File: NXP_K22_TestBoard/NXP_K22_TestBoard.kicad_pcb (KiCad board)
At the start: 4 copper layers, 60 x 90 mm, 63 parts, among them J301 Barrel_Jack, J302 Conn_ARM_JTAG_SWD_10, J303 PortA, J304 PortB, J305 PortC, J306 PortD, J307 Analog, J308 OLED, J309 UART, J310 Power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

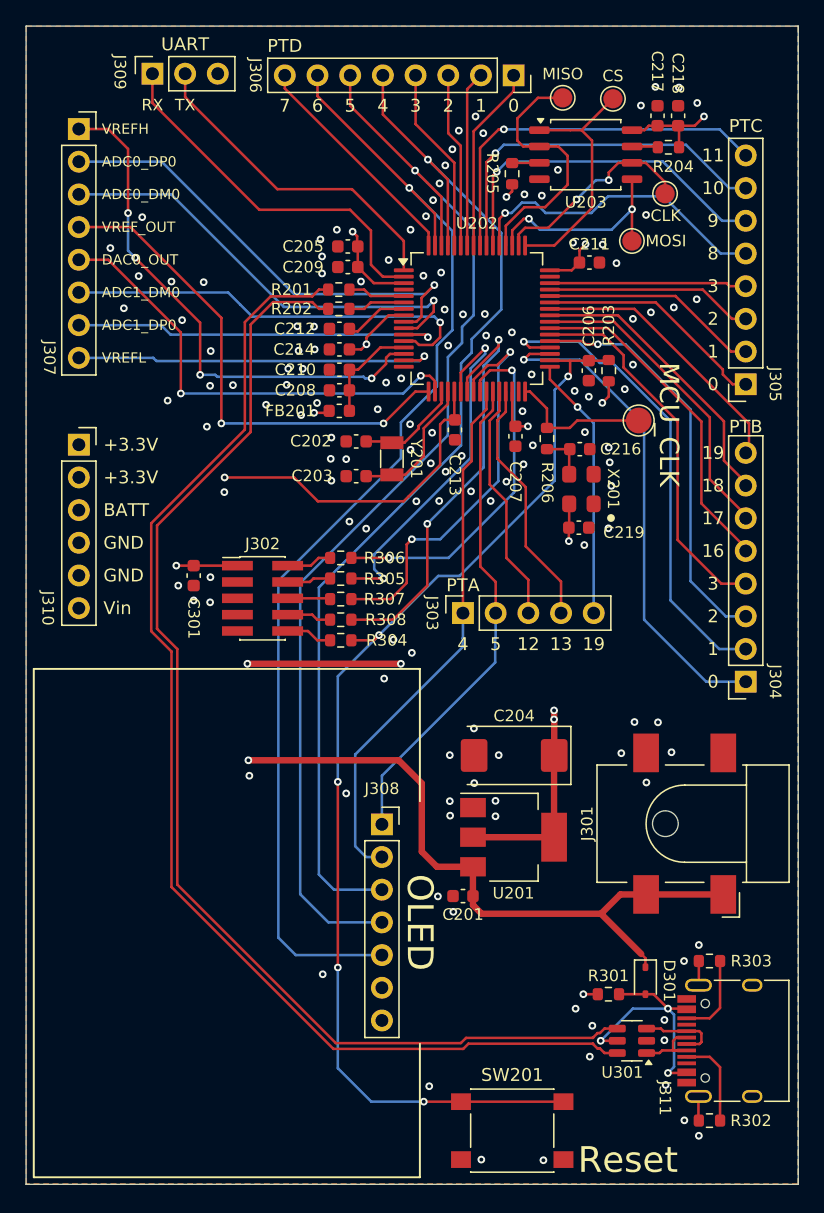
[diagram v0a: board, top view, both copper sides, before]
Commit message: Finished board layout
Design rules not checked yet
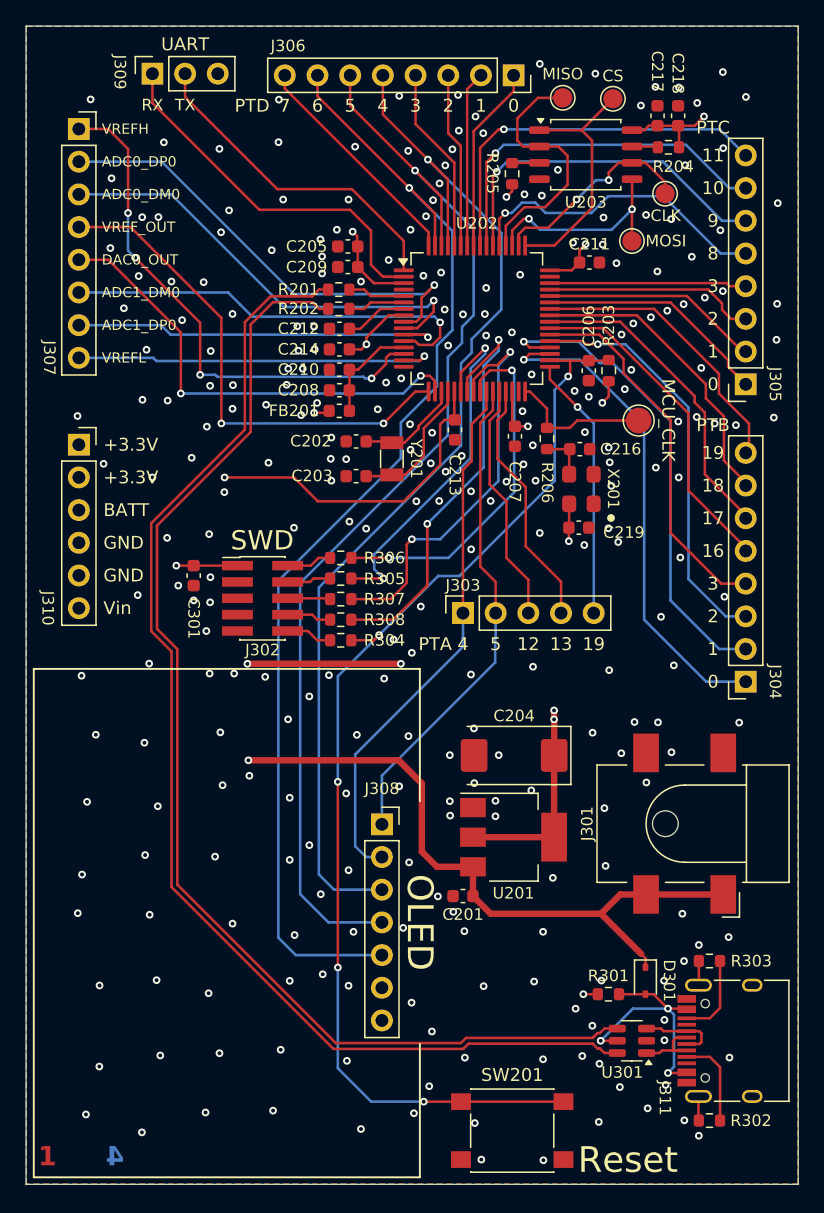
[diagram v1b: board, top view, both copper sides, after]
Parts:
- added REF**: Symbol_Barrel_Polarity, Symbol:Symbol_Barrel_Polarity, B.Cu at (144.3, 94.8)
- C202, C203: value C -> 20p
- C217: value 1nF -> 1n
- C218: value 100nF -> 100n
- C301: value C -> 100n
- Y201: value Crystal -> 32.768 kHz
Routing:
- net PTC2: track 16.3 -> 17.2 mm
- net PTB19: track 21.4 -> 22.3 mm
- net PTB18: track 22.7 -> 23.5 mm
- net GND: vias 133 -> 274
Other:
- board text added: "+"
- board text added: "-"
- board text added: "NXP MK22FN512 Test board V1.0 by Morgan ON4MOD"
- board text added: "SWD"

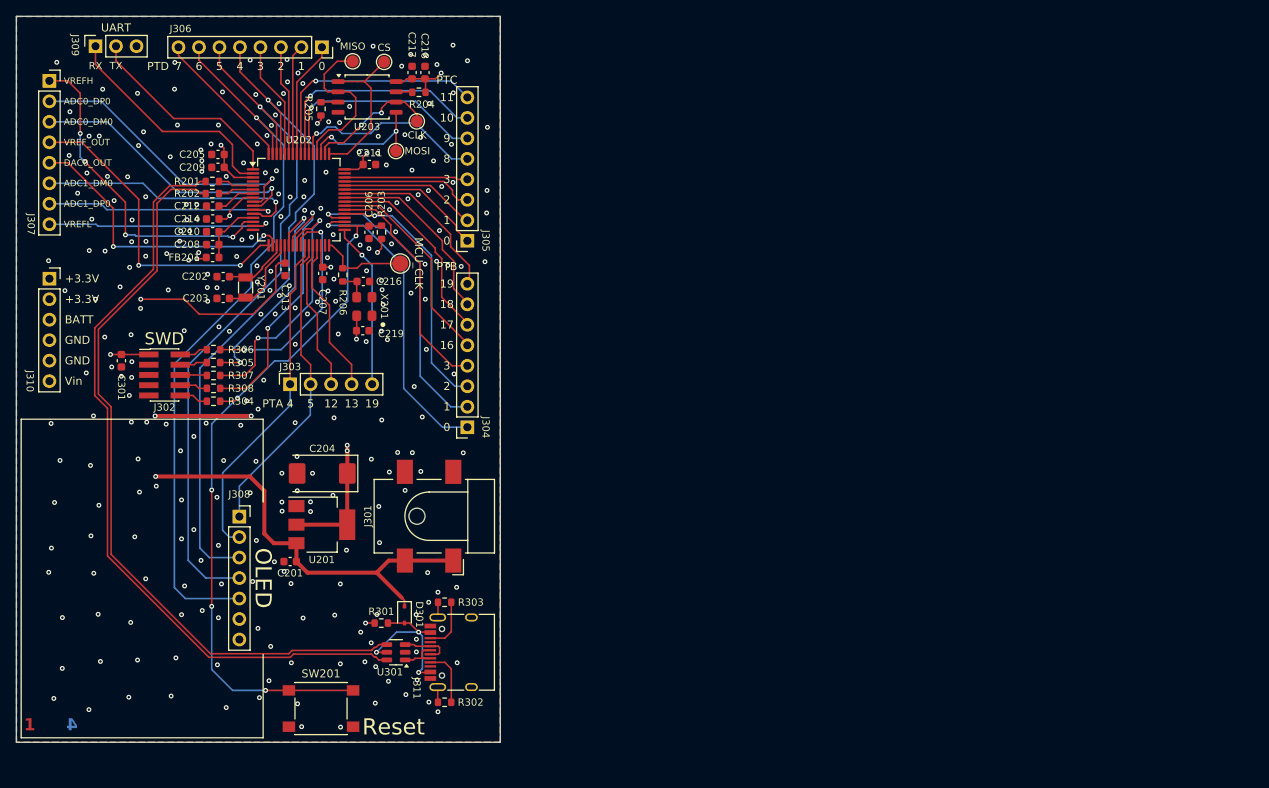
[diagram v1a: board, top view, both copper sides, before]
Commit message: Finishing touches
Set manufacturing constraints to JLCPCB constraints, set USB differential pair to correct width/spacing.
Set-up pcb characteristics, added descriptions to user comments layer, fixed power regulator footprint being outdated.
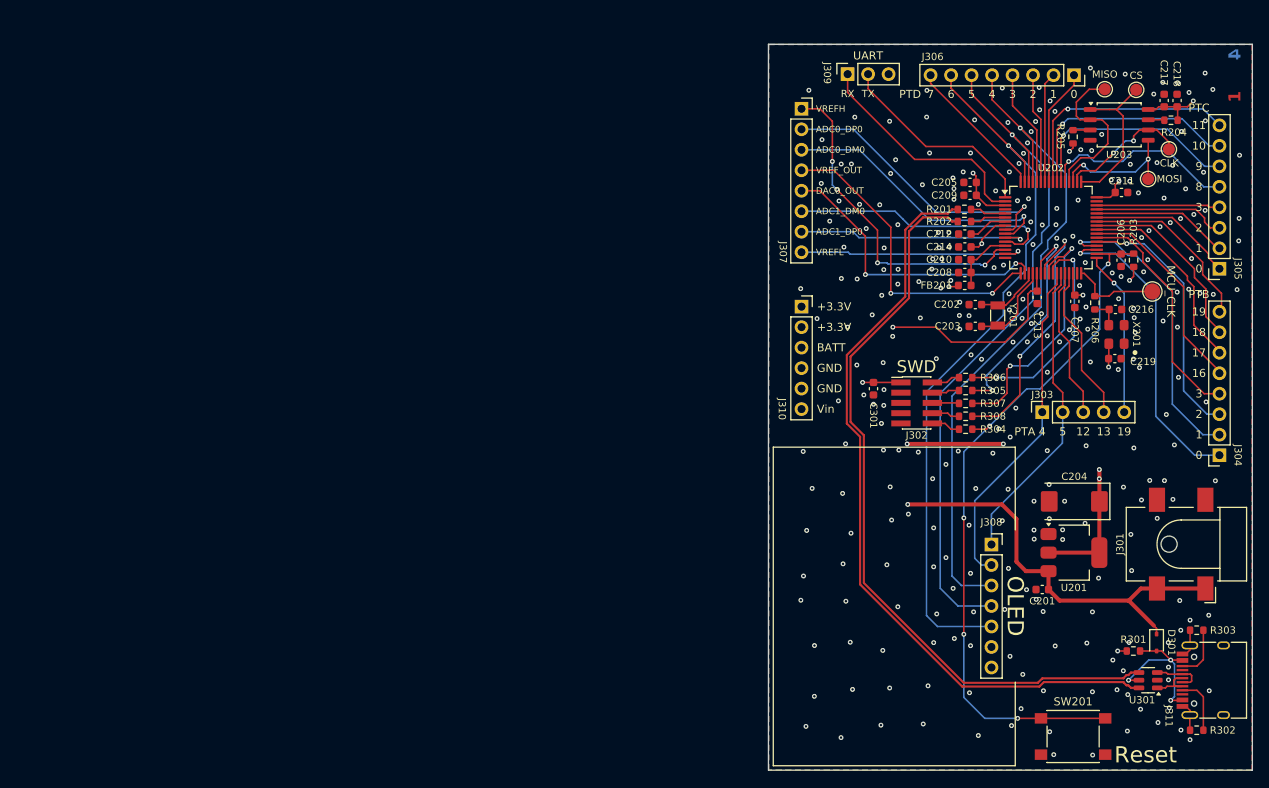
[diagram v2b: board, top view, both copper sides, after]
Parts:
- moved C208 93.3 mm to (204.2, 64.6)
- moved C210 93.3 mm to (204.2, 63.0)
- moved C212 93.3 mm to (204.2, 59.9)
- moved C214 93.3 mm to (204.2, 61.5)
- moved J306 93.3 mm to (217.7, 40.2)
- moved J307 93.3 mm to (183.9, 44.3)
- moved R205 93.3 mm to (217.6, 47.8)
- moved R206 93.3 mm to (220.3, 68.4)
- moved C201 93.3 mm to (213.8, 103.9)
- moved C202 93.3 mm to (205.5, 68.6)
- moved C203 93.3 mm to (205.5, 71.3)
- moved C204 93.3 mm to (217.7, 93.0)
- moved C206 93.3 mm to (223.5, 63.1)
- moved C207 93.3 mm to (217.8, 68.2)
- moved C211 93.3 mm to (223.6, 54.7)
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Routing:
- net GND: track 3.78 -> 7.15 mm
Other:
- board text added: "0 mm"
- board text added: "0.01 mm"
- board text added: "0.0152 mm"
- board text added: "0.02"
- board text added: "0.035 mm"
- board text added: "0.1000 mm / 0.1000 mm"
- board text added: "0.2104 mm"
- board text added: "0.3000 mm"
- board text added: "1.065 mm"
- board text added: "1.6062 mm"
- board text added: "3.3"
- board text added: "4.4"
- board text added: "4.5"
- board text added: "60.0000 mm x 90.0000 mm"
- board text added: "7628"
- board text added: "B.Cu"
- board text added: "B.Mask"
- board text added: "B.Paste"
- board text added: "B.Silkscreen"
- board text added: "BOARD CHARACTERISTICS"
- board text added: "Board Thickness:"
- board text added: "Board overall dimensions:"
- board text added: "Bottom Silk Screen"
- board text added: "Bottom Solder Mask"
- board text added: "Bottom Solder Paste"
- board text added: "Castellated pads:"
- board text added: "Color"
- board text added: "Copper Finish:"
- board text added: "Copper Layer Count:"
- board text added: "Dielectric 1"
- board text added: "Dielectric 2"
- board text added: "Dielectric 3"
- board text added: "Edge card connectors:"
- board text added: "Epsilon R"
- board text added: "F.Cu"
- board text added: "F.Mask"
- board text added: "F.Paste"
- board text added: "F.Silkscreen"
- board text added: "FR4"
- board text added: "FR4 natural"
- board text added: "Green"
- board text added: "Impedance Control:"
- board text added: "In1.Cu"
- board text added: "In2.Cu"
- board text added: "Layer Name"
- board text added: "Loss Tangent"
- board text added: "Material"
- board text added: "Min hole diameter:"
- board text added: "Min track/spacing:"
- board text added: "No"
- board text added: "Not specified"
- board text added: "Plated Board Edge:"
- board text added: "Thickness (mm)"
- board text added: "Top Silk Screen"
- board text added: "Top Solder Mask"
- board text added: "Top Solder Paste"
- board text added: "Type"
- board text added: "White"
- board text added: "copper"
- board text added: "core"
- board text added: "prepreg"
